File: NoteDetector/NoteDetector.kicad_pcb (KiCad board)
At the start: 2 copper layers, 25.4 x 25.4 mm, 49 parts, among them J1 Conn_01x01, J2 Conn_01x01, J3 Conn_01x01, J4 Conn_01x01, J5 Conn_01x01, J6 Conn_01x01, J7 Conn_01x01, Q1 Q_NMOS_DGS, Q2 Q_NMOS_DGS, Q3 Q_NMOS_DGS, Q4 Q_NMOS_DGS, U1 OPAMP, U2 PIC18F06

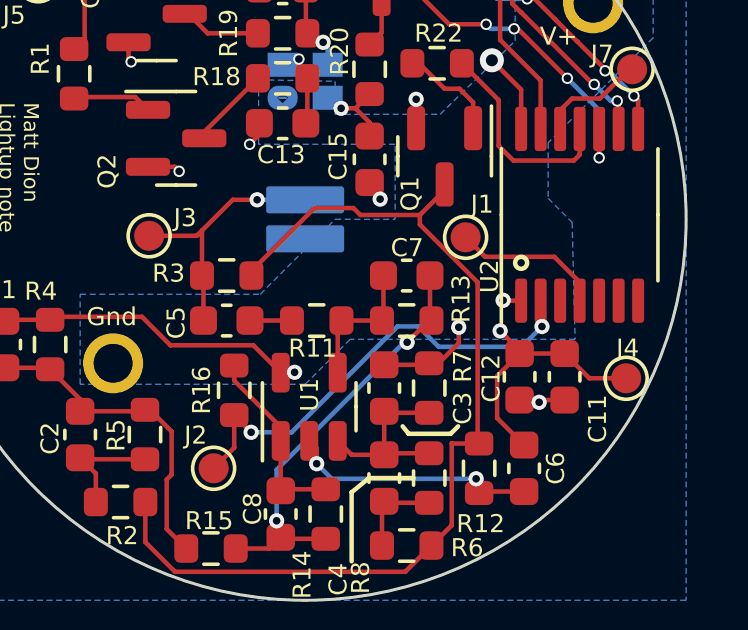
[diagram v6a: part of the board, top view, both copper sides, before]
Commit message: Tweaked layout to get better clearance around programming contact
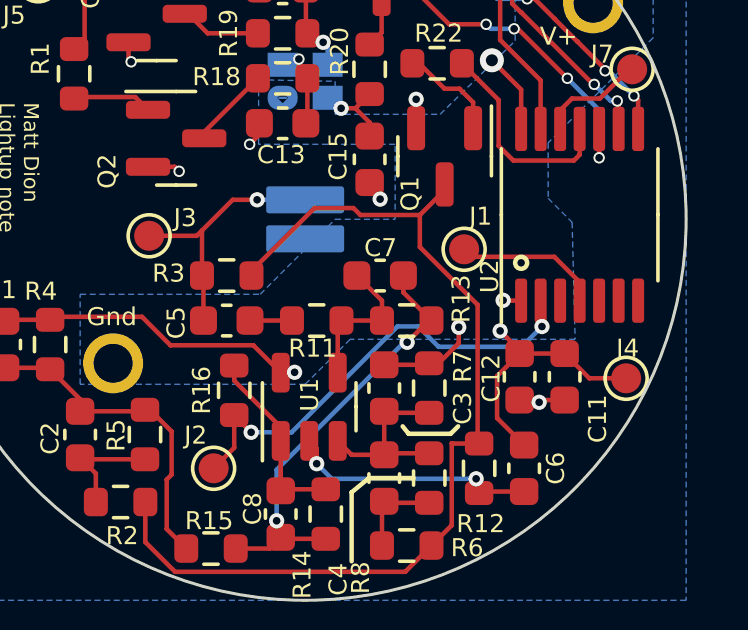
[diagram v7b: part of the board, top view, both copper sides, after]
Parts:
- moved C7 0.89 mm to (2.50, 1.88)
- moved J1 0.40 mm to (5.30, 1.00)
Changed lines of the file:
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@@
   )
   (footprint "TestPoint:TestPoint_Pad_D1.0mm" (layer "F.Cu")
-    (at 5.35 0.6)
+    (at 5.3 1)
     (descr "SMD pad as test Point, diameter 1.0mm")
     (tags "test point SMD pad")
@@
   )
   (footprint "Capacitor_SMD:C_0603_1608Metric" (layer "F.Cu")
-    (at 3.386384 1.875 180)
+    (at 2.5 1.875 180)
     (descr "Capacitor SMD 0603 (1608 Metric), square (rectangular) end terminal, IPC_7351 nominal, (Body size source: IPC-SM-782 page 76, https://www.pcb-3d.com/wordpress/wp-content/uploads/ipc-sm-782a_amendment_1_and_2.pdf), generated with kicad-footprint-generator")
     (tags "capacitor")
@@
   (segment (start 3.4 4.1) (end 4.125 3.375) (width 0.1524) (layer "F.Cu") (net 10))
   (segment (start -2.313616 10.975) (end -1.188616 10.975) (width 0.1524) (layer "F.Cu") (net 10))
-  (segment (start 4.161384 1.875) (end 4.161384 3.325) (width 0.1524) (layer "F.Cu") (net 10))
-  (segment (start 4.161384 3.325) (end 4.211384 3.375) (width 0.1524) (layer "F.Cu") (net 10))
+  (segment (start 3.275 1.875) (end 3.275 2.438616) (width 0.1524) (layer "F.Cu") (net 10))
   (segment (start 0.686384 10.65) (end -0.763616 10.65) (width 0.1524) (layer "F.Cu") (net 10))
   (segment (start 4.125 3.375) (end 4.211384 3.375) (width 0.1524) (layer "F.Cu") (net 10))
   (segment (start -0.95 10.463616) (end -0.813616 10.6) (width 0.1524) (layer "F.Cu") (net 10))
   (segment (start -0.763616 10.65) (end -0.813616 10.6) (width 0.1524) (layer "F.Cu") (net 10))
+  (segment (start 3.275 2.438616) (end 4.211384 3.375) (width 0.1524) (layer "F.Cu") (net 10))
   (segment (start -1.188616 10.975) (end -0.813616 10.6) (width 0.1524) (layer "F.Cu") (net 10))
   (segment (start -0.95 10.05) (end -0.95 10.463616) (width 0.1524) (layer "F.Cu") (net 10))
@@
   (segment (start 1.086384 3.5) (end 1.211384 3.375) (width 0.1524) (layer "F.Cu") (net 11))
   (segment (start 1.211384 3.375) (end 2.561384 3.375) (width 0.1524) (layer "F.Cu") (net 11))
-  (segment (start 2.611384 1.875) (end 2.611384 3.325) (width 0.1524) (layer "F.Cu") (net 11))
   (segment (start 1.086384 5.1125) (end 1.086384 3.5) (width 0.1524) (layer "F.Cu") (net 11))
-  (segment (start 2.611384 3.325) (end 2.561384 3.375) (width 0.1524) (layer "F.Cu") (net 11))
+  (segment (start 1.725 1.875) (end 2.561384 2.711384) (width 0.1524) (layer "F.Cu") (net 11))
+  (segment (start 2.561384 2.711384) (end 2.561384 3.375) (width 0.1524) (layer "F.Cu") (net 11))
   (segment (start 5.425 -7.7) (end 5.1 -8.025) (width 0.1524) (layer "F.Cu") (net 12))
   (segment (start 6 -7.7) (end 5.425 -7.7) (width 0.1524) (layer "F.Cu") (net 12))
@@
   (segment (start 4.64808 -4.35192) (end 5.14577 -4.35192) (width 0.1524) (layer "F.Cu") (net 16))
   (segment (start 3.8 -5.2) (end 4.64808 -4.35192) (width 0.1524) (layer "F.Cu") (net 16))
-  (segment (start 6 1.25) (end 8.306348 1.25) (width 0.1524) (layer "F.Cu") (net 18))
+  (segment (start 8.306348 1.25) (end 9.15 2.093652) (width 0.1524) (layer "F.Cu") (net 18))
+  (segment (start 5.3 1) (end 5.55 1.25) (width 0.1524) (layer "F.Cu") (net 18))
   (segment (start 9.15 2.093652) (end 9.15 2.7125) (width 0.1524) (layer "F.Cu") (net 18))
-  (segment (start 8.306348 1.25) (end 9.15 2.093652) (width 0.1524) (layer "F.Cu") (net 18))
-  (segment (start 5.35 0.6) (end 6 1.25) (width 0.1524) (layer "F.Cu") (net 18))
+  (segment (start 5.55 1.25) (end 8.306348 1.25) (width 0.1524) (layer "F.Cu") (net 18))
   (segment (start -0.813616 9.05) (end -0.813616 7.3875) (width 0.1524) (layer "F.Cu") (net 19))
   (segment (start -0.763616 9) (end -0.813616 9.05) (width 0.1524) (layer "F.Cu") (net 19))
@@
   (segment (start -5.326116 9.425) (end -5.326116 10.760269) (width 0.1524) (layer "F.Cu") (net 23))
   (segment (start -4.336385 11.75) (end 3.336384 11.75) (width 0.1524) (layer "F.Cu") (net 23))
+  (segment (start 3.824565 -0.142634) (end 3.824565 0.924565) (width 0.1524) (layer "F.Cu") (net 23))
   (segment (start 4.65 -1.1625) (end 4.65 -0.968069) (width 0.1524) (layer "F.Cu") (net 23))
   (segment (start 5.8 7.475) (end 4.899208 7.475) (width 0.1524) (layer "F.Cu") (net 23))
   (segment (start 4.899208 7.475) (end 4.887104 7.462896) (width 0.1524) (layer "F.Cu") (net 23))
-  (segment (start 5.75 2.1) (end 5.75 7.425) (width 0.1524) (layer "F.Cu") (net 23))
-  (segment (start 3.824565 0.174565) (end 5.75 2.1) (width 0.1524) (layer "F.Cu") (net 23))
-  (segment (start 5.75 7.425) (end 5.8 7.475) (width 0.1524) (layer "F.Cu") (net 23))
+  (segment (start 3.824565 0.924565) (end 5.75 2.85) (width 0.1524) (layer "F.Cu") (net 23))
+  (segment (start 5.75 2.85) (end 5.75 7.425) (width 0.1524) (layer "F.Cu") (net 23))
   (segment (start 3.336384 11.75) (end 4.211384 10.875) (width 0.1524) (layer "F.Cu") (net 23))
   (segment (start 4.65 -0.968069) (end 3.824565 -0.142634) (width 0.1524) (layer "F.Cu") (net 23))
   (segment (start 4.887104 7.462896) (end 4.887104 10.19928) (width 0.1524) (layer "F.Cu") (net 23))
-  (segment (start 3.824565 -0.142634) (end 3.824565 0.174565) (width 0.1524) (layer "F.Cu") (net 23))
+  (segment (start 5.75 7.425) (end 5.8 7.475) (width 0.1524) (layer "F.Cu") (net 23))
   (segment (start -3.25 -6.2) (end -1.575 -6.2) (width 0.1524) (layer "F.Cu") (net 24))
   (segment (start -4.0125 -6.85) (end -3.9 -6.85) (width 0.1524) (layer "F.Cu") (net 24))

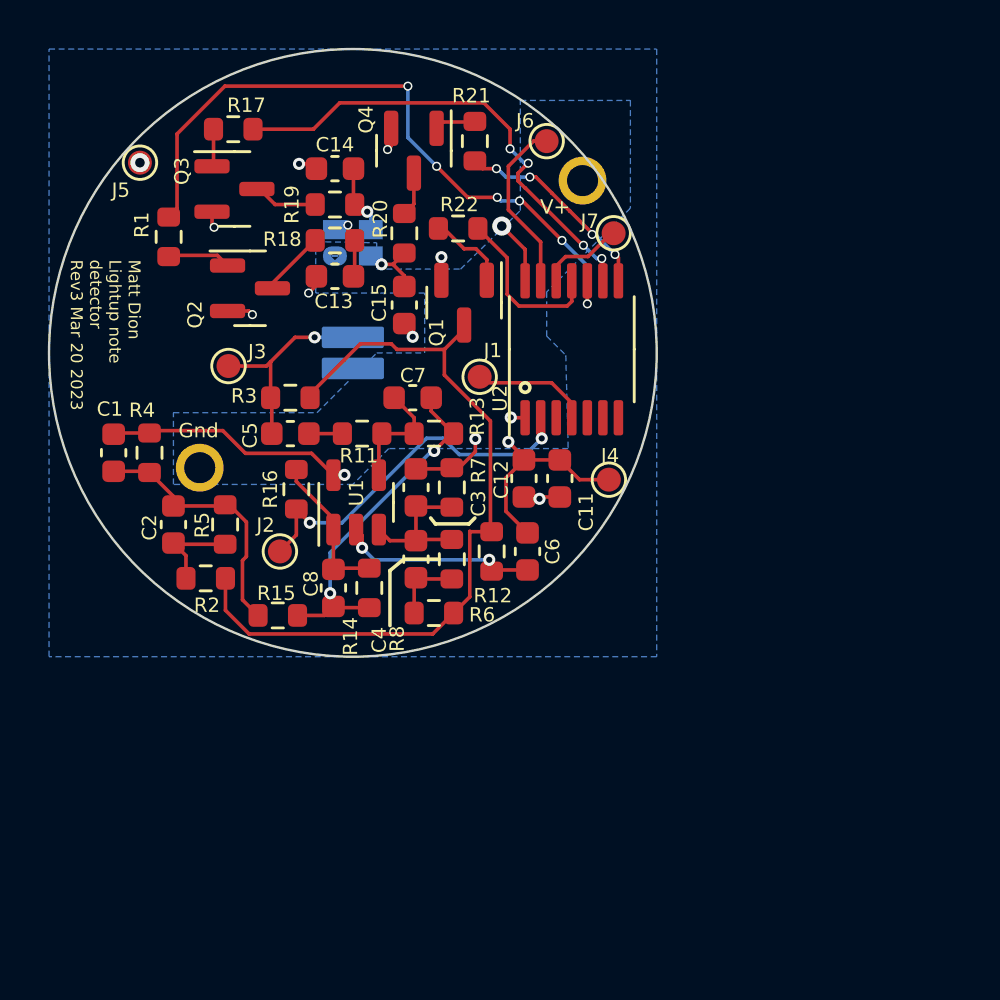
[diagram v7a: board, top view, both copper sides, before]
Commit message: Changelog: combined midscale references; added reverse voltage protection; moved ~MCLR programming pad to board perimeter; increased min drill/pad size
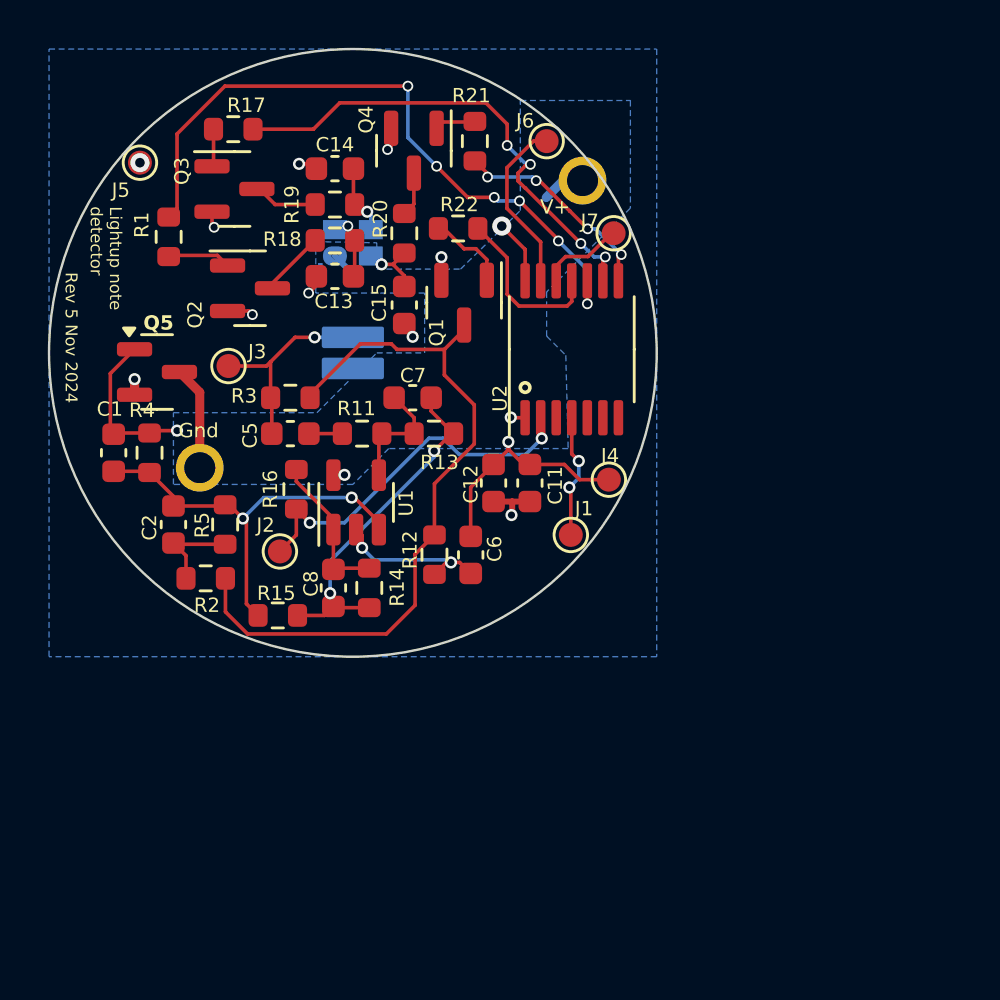
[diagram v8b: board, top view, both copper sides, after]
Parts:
- removed C3, C4: 1n, Capacitor_SMD:C_0603_1608Metric
- removed R6: 1k, Resistor_SMD:R_0603_1608Metric
- removed R7, R8: 10M, Resistor_SMD:R_0603_1608Metric
- added Q5: Q_NMOS_DGS, Package_TO_SOT_SMD:SOT-23, F.Cu at (-8.19, 0.80)
- C5: value C_in -> 10n
- C7, C8: value C_fb -> 10p
- moved J1 7.63 mm to (9.11, 7.61)
- moved R12 2.39 mm to (3.41, 8.44)
- moved C6 2.38 mm to (4.92, 8.45)
- moved C12 1.28 mm to (5.88, 5.44)
- moved C11 1.26 mm to (7.40, 5.44)
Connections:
- BT1 pad 2: GND -> /PGnd
- C1 pad 1: /Midscale2 -> /Midscale
- C2 pad 2: /Midscale2 -> /Midscale
- R15 pad 2: /Midscale2 -> /Midscale
- R4 pad 1: /Midscale2 -> /Midscale
- R5 pad 2: /Midscale2 -> /Midscale
- U1 pad 3: /Midscale1 -> /Midscale
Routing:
- net /Midscale: track 0.00 -> 17.6 mm, vias 0 -> 2
- net /Midscale2: track 10.9 -> 0.00 mm
- net /Midscale1: track 6.23 -> 0.00 mm
- net /PGnd: track 0.00 -> 4.35 mm
- net Net-(C4-Pad1): track 3.03 -> 0.00 mm
- net +BATT: track 23.0 -> 20.6 mm
- net /gnd_switch: track 32.8 -> 30.5 mm
- net Net-(U1-V-): track 8.42 -> 6.74 mm
- net GND: track 10.3 -> 11.5 mm, vias 10 -> 11
- net /~{MCLR}: track 4.92 -> 5.21 mm, vias 0 -> 2
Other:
- board text added: "."
- board text added: "Lightup note detector"
- board text added: "Rev 5 Nov 2024"
- board text removed: "Matt Dion Lightup note detector Rev3 Mar 20 2023"
